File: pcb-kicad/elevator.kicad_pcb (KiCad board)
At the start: 2 copper layers, 147 parts, among them Q1 AO3416, SW1 MX-with-LED, SW10 MX-with-LED, SW11 MX-with-LED, SW12 MX-with-LED, SW13 MX-with-LED, SW14 MX-with-LED, SW15 MX-with-LED, SW16 MX-with-LED, SW17 MX-with-LED, SW18 MX-with-LED, SW19 MX-with-LED, SW2 MX-with-LED, SW20 MX-with-LED, SW21 MX-with-LED, SW22 MX-with-LED, SW23 MX-with-LED, SW24 MX-with-LED, SW25 MX-with-LED, SW26 MX-with-LED, SW27 MX-with-LED, SW28 MX-with-LED, SW29 MX-with-LED, SW3 MX-with-LED, SW30 MX-with-LED, SW31 MX-with-LED, SW32 MX-with-LED, SW33 MX-with-LED, SW34 MX-with-LED, SW35 MX-with-LED, SW36 MX-with-LED, SW37 MX-with-LED, SW38 MX-with-LED, SW39 MX-with-LED, SW4 MX-with-LED, SW40 MX-with-LED, SW41 MX-with-LED, SW42 MX-with-LED, SW43 MX-with-LED, SW44 MX-with-LED, SW45 MX-with-LED, SW46 MX-with-LED, SW47 MX-with-LED, SW48 MX-with-LED, SW5 MX-with-LED, SW6 MX-with-LED, SW7 MX-with-LED, SW8 MX-with-LED, SW9 MX-with-LED, U1 Frood

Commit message: Route switch matrix and couple other things
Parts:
- D1, D10, D11, D12, D13, D14, D15, D16, D17, D18, D19, D2, D20, D21, D22, D23, D24, D25, D26, D27, D28, D29, D3, D30, D31, D32, D33, D34, D35, D36, D37, D38, D39, D4, D40, D41, D42, D43, D44, D45, D46, D47, D48, D5, D6, D7, D8, D9, R1, R10, R11, R12, R13, R14, R15, R16, R17, R18, R19, R2, R20, R21, R22, R23, R24, R25, R26, R27, R28, R29, R3, R30, R31, R32, R33, R34, R35, R36, R37, R38, R39, R4, R40, R41, R42, R43, R44, R45, R46, R47, R48, R5, R6, R7, R8, R9: moved to B.Cu
- moved D12 279.1 mm to (265.9, 45.9), turned to -90 degrees
- moved D11 261.5 mm to (246.9, 45.9), turned to -90 degrees
- moved D24 259.4 mm to (265.9, 65.0), turned to -90 degrees
- moved R12 249.7 mm to (274.6, 54.8), turned to 180 degrees
- moved D10 244.1 mm to (227.8, 45.9), turned to -90 degrees
- moved D23 241.4 mm to (246.9, 65.0), turned to -90 degrees
- moved D36 240.5 mm to (265.9, 84.0), turned to -90 degrees
- moved SW12 237.5 mm to (274.5, 46.8)
- moved R11 232.2 mm to (255.5, 54.8), turned to 180 degrees
- moved R24 230.6 mm to (274.6, 73.8), turned to 180 degrees
- moved D9 227.0 mm to (208.8, 45.9), turned to -90 degrees
- moved D22 223.6 mm to (227.8, 65.0), turned to -90 degrees
- moved D48 222.6 mm to (265.9, 103.1), turned to -90 degrees
- moved D35 222.1 mm to (246.9, 84.0), turned to -90 degrees
- moved R10 215.1 mm to (236.5, 54.8), turned to 180 degrees
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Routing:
- net /LED_D: track 0.00 -> 978.5 mm
- net /ROW1: track 0.00 -> 212.6 mm
- net /ROW5: track 0.00 -> 212.3 mm
- net /ROW3: track 0.00 -> 212.3 mm
- net /ROW7: track 0.00 -> 212.3 mm
- net /ROW6: track 0.00 -> 195.1 mm
- net /ROW4: track 0.00 -> 195.1 mm
- net /ROW2: track 0.00 -> 195.1 mm
- net /ROW0: track 0.00 -> 195.1 mm
- net /COL0: track 0.00 -> 157.5 mm
- net /COL5: track 0.00 -> 152.6 mm
- net /COL1: track 0.00 -> 152.6 mm
- net /COL4: track 0.00 -> 152.6 mm
- net /COL3: track 0.00 -> 152.6 mm
- net /COL2: track 0.00 -> 152.6 mm
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
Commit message: Route LEDs
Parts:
- moved U1 2.62 mm to (42.5, 38.9)
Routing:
- net /VCC: track 0.00 -> 886.1 mm

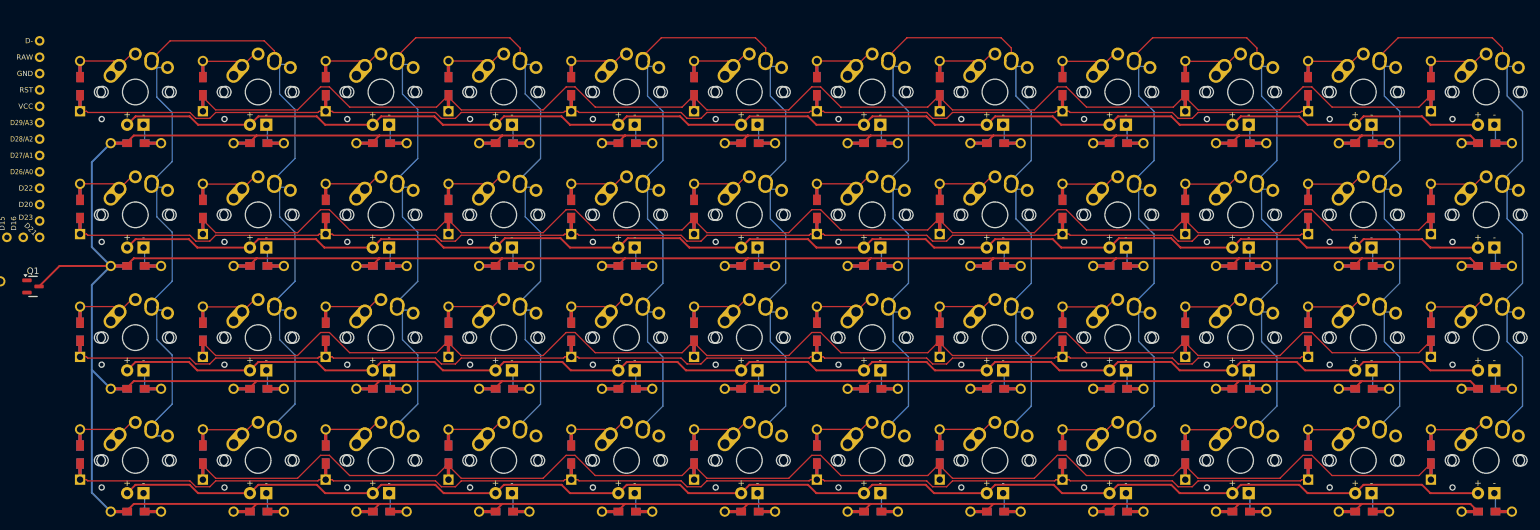
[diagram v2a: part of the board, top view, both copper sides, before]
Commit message: Finish LED routing, route columns to the controller
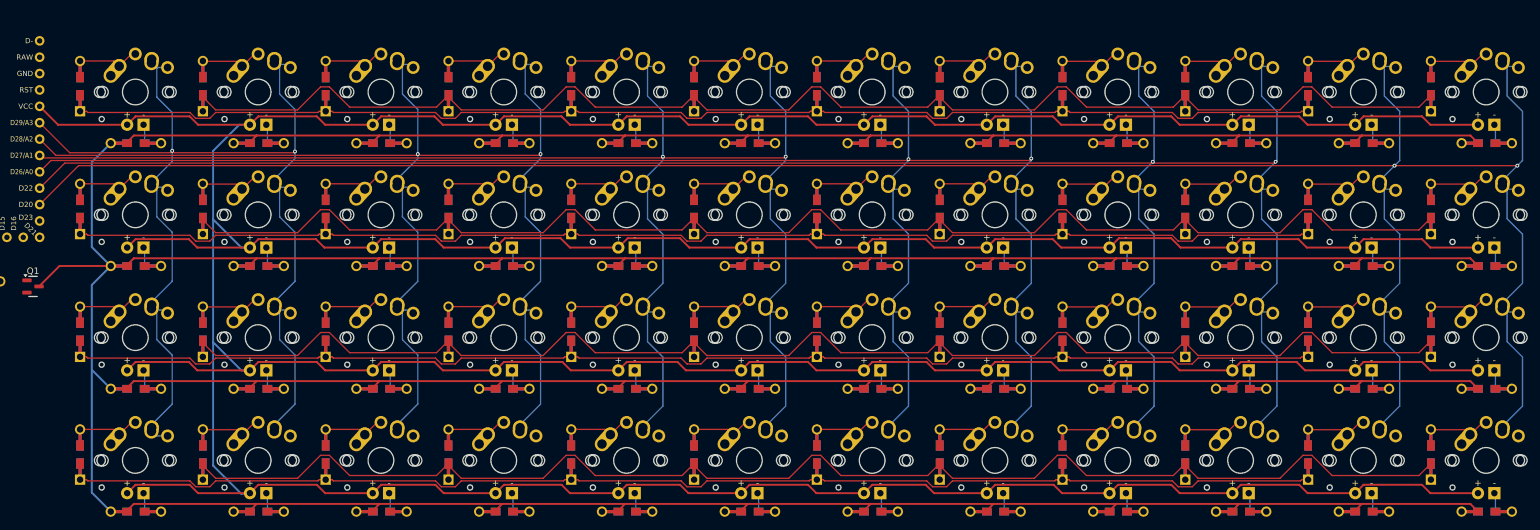
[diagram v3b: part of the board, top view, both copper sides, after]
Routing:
- net /COL5: track 152.6 -> 362.2 mm, vias 0 -> 2
- net /COL4: track 152.6 -> 324.0 mm, vias 0 -> 2
- net /COL3: track 152.6 -> 285.3 mm, vias 0 -> 2
- net /COL2: track 152.6 -> 246.7 mm, vias 0 -> 2
- net /VCC: track 886.1 -> 979.5 mm
- net /COL1: track 152.6 -> 209.4 mm, vias 0 -> 2
- net /COL0: track 157.5 -> 177.3 mm, vias 0 -> 2

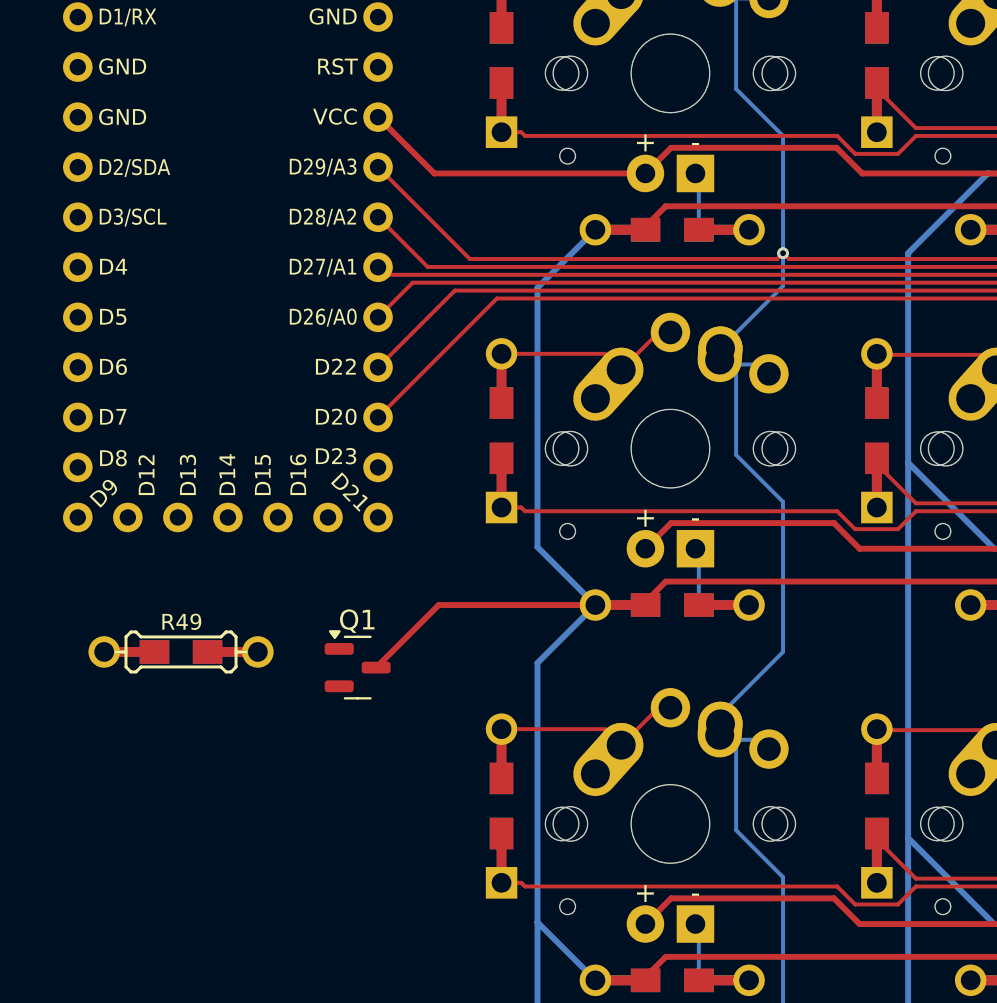
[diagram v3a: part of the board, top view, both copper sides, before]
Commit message: Some wirint, add fp-lib-table to .gitignore
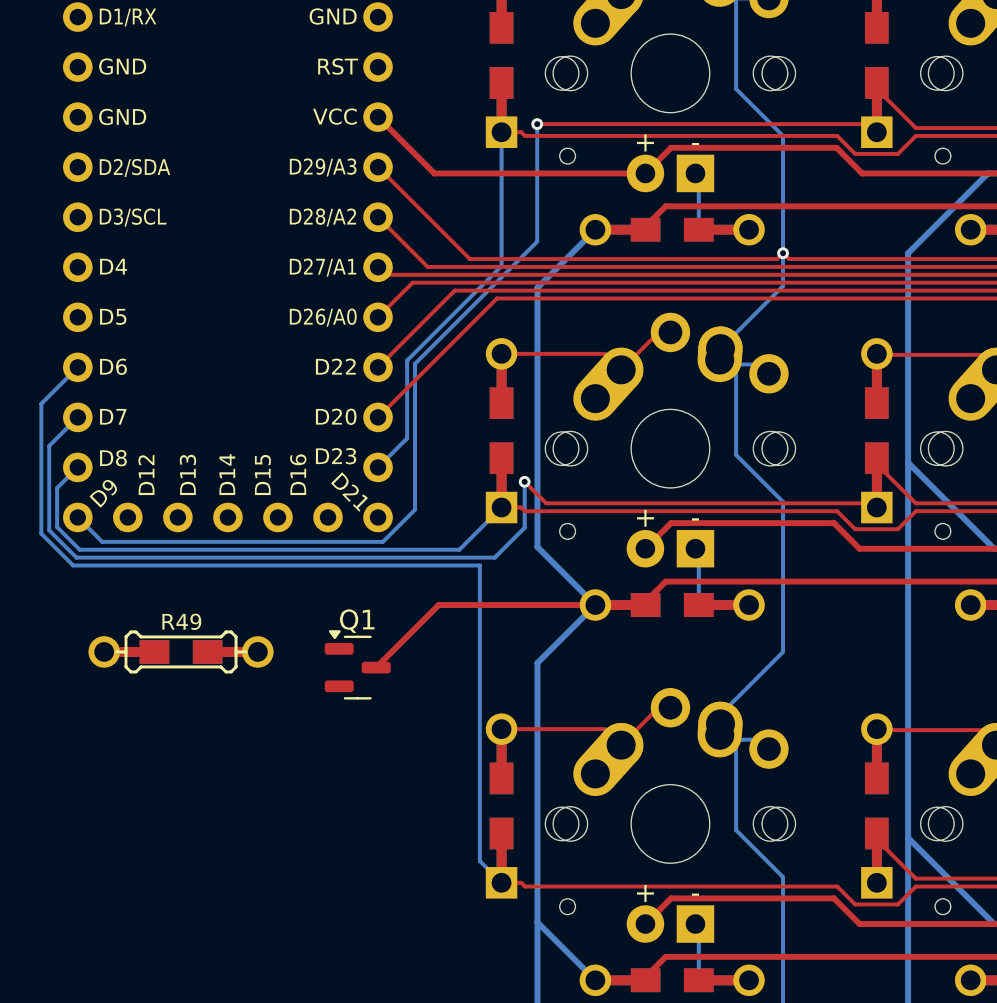
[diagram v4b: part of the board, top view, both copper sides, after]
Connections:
- U1 pad 10: /ROW6 -> /ROW4
- U1 pad 11: /ROW7 -> /ROW3
- U1 pad 12: unconnected-(U1-GPIO8-Pad12) -> /ROW2
- U1 pad 13: unconnected-(U1-GPIO9-Pad13) -> /ROW1
- U1 pad 2: /ROW0 -> /ROW7
- U1 pad 20: unconnected-(U1-GPIO23-Pad20) -> /ROW0
- U1 pad 3: /ROW1 -> /ROW6
- U1 pad 6: /ROW2 -> unconnected-(U1-GPIO2-Pad6)
- U1 pad 7: /ROW3 -> unconnected-(U1-GPIO3-Pad7)
- U1 pad 8: /ROW4 -> /ROW5
- U1 pad 9: /ROW5 -> unconnected-(U1-GPIO5-Pad9)
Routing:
- net /ROW1: track 212.6 -> 271.3 mm, vias 0 -> 1
- net /ROW3: track 212.3 -> 264.8 mm, vias 0 -> 1
- net /ROW4: track 195.1 -> 243.8 mm
- net /ROW2: track 195.1 -> 222.4 mm
- net /ROW0: track 195.1 -> 214.7 mm

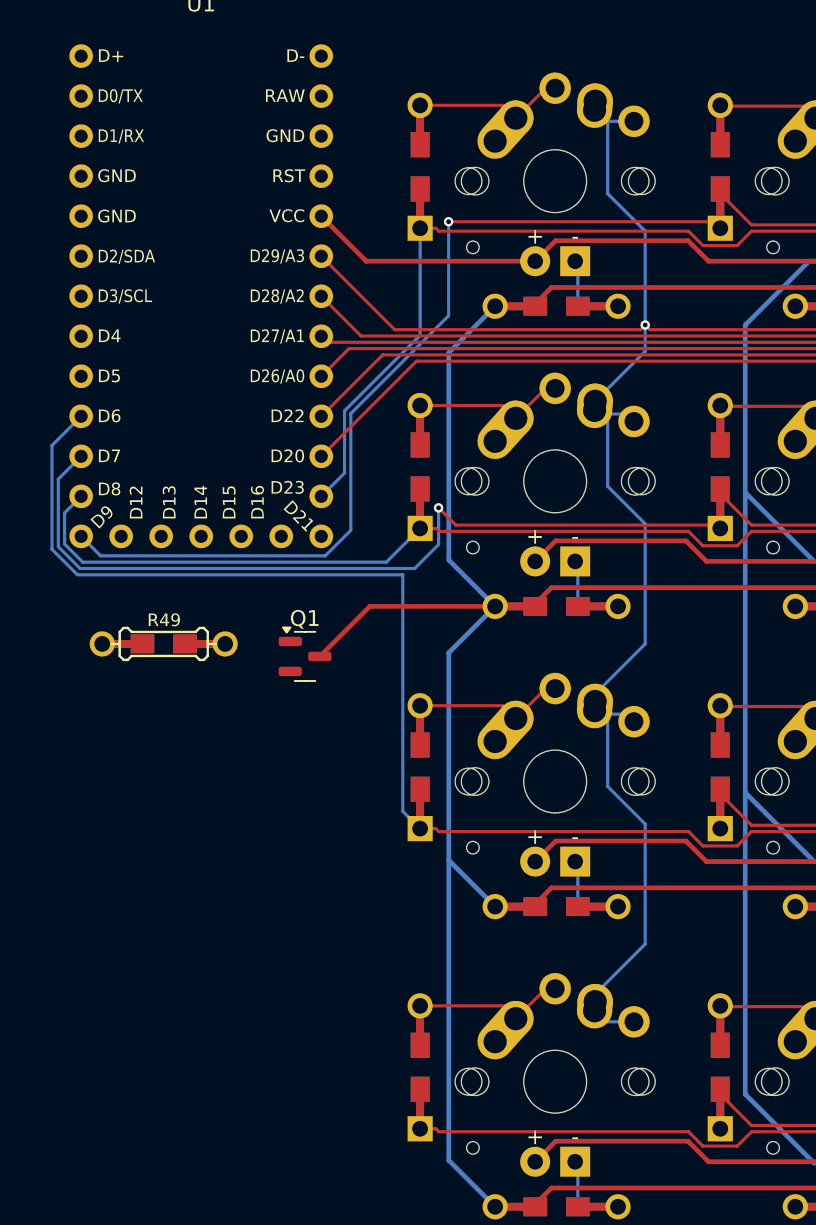
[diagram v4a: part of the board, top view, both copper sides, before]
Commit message: Finish matrix wiring, add encoder schematic
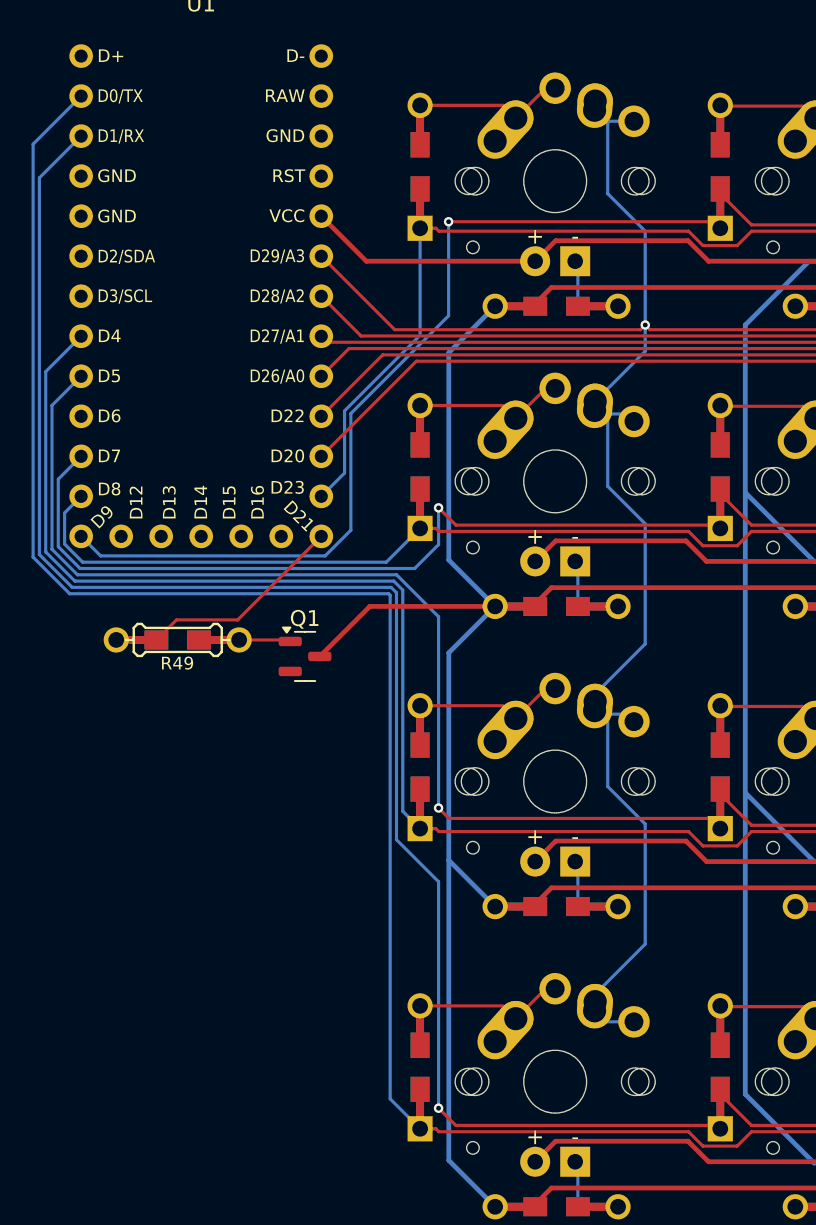
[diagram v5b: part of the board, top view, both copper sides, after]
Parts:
- moved R49 0.92 mm to (41.0, 75.9), turned to 0 degrees
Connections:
- U1 pad 10: /ROW4 -> unconnected-(U1-GPIO6-Pad10)
- U1 pad 2: /ROW7 -> /ROW6
- U1 pad 3: /ROW6 -> /ROW7
- U1 pad 8: /ROW5 -> /ROW4
- U1 pad 9: unconnected-(U1-GPIO5-Pad9) -> /ROW5
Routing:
- net /ROW7: track 212.3 -> 315.9 mm, vias 0 -> 1
- net /ROW6: track 195.1 -> 283.9 mm
- net /ROW5: track 212.3 -> 280.9 mm, vias 0 -> 1
- net /LED_PWM: track 0.00 -> 13.2 mm
- net /ROW4: track 243.8 -> 248.9 mm
- net Net-(Q1-G): track 0.00 -> 3.28 mm

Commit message: Add rotary encoder circuitry to the PCB
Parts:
- added C1: 100n, Capacitor_THT:C_Disc_D4.3mm_W1.9mm_P5.00mm, F.Cu at (38.6, 103.2)
- added C2: 100n, Capacitor_THT:C_Disc_D4.3mm_W1.9mm_P5.00mm, F.Cu at (45.7, 103.2)
- added D49: D_Small, Keebio-Parts:Diode-dual, F.Cu at (52.1, 95.4)
- added R50: 10k, Keebio-Parts:Resistor-Hybrid, F.Cu at (36.8, 95.5)
- added R51: 10k, Keebio-Parts:Resistor-Hybrid, F.Cu at (40.4, 95.5)
- added R52: 10k, Keebio-Parts:Resistor-Hybrid, F.Cu at (43.9, 95.5)
- added R53: 10k, Keebio-Parts:Resistor-Hybrid, F.Cu at (47.5, 95.5)
- added SW49: RotaryEncoder_Switch, Rotary_Encoder:RotaryEncoder_Alps_EC11E-Switch_Vertical_H20mm, F.Cu at (42.4, 73.3)
- moved R49 10.7 mm to (51.6, 77.7), turned to -90 degrees
- moved Q1 9.21 mm to (51.6, 85.9), turned to -90 degrees
- moved D11 1.79 mm to (247.4, 44.2)
- moved D15 1.79 mm to (95.0, 63.3)
- moved D16 1.79 mm to (114.0, 63.3)
- moved D18 1.79 mm to (152.1, 63.3)
- moved D19 1.79 mm to (171.2, 63.3)
- moved D21 1.79 mm to (209.3, 63.3)
- moved D23 1.79 mm to (247.4, 63.3)
- moved D27 1.79 mm to (95.0, 82.3)
- moved D28 1.79 mm to (114.0, 82.3)
- moved D3 1.79 mm to (95.0, 44.2)
- moved D30 1.79 mm to (152.1, 82.3)
- moved D31 1.79 mm to (171.2, 82.3)
- moved D33 1.79 mm to (209.3, 82.3)
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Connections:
- net /GND renamed GND
- net /VCC renamed VCC
- U1 pad 10: unconnected-(U1-GPIO6-Pad10) -> /COL6
- U1 pad 6: unconnected-(U1-GPIO2-Pad6) -> /ENC1
- U1 pad 7: unconnected-(U1-GPIO3-Pad7) -> /ENC2
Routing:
- net /LED_PWM: track 13.2 -> 0.00 mm
- net /LED_D: track 978.5 -> 966.0 mm
- net Net-(Q1-G): track 3.28 -> 0.00 mm
